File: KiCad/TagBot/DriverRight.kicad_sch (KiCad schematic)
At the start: 3 parts, among them U301 ZXBM5210-SP

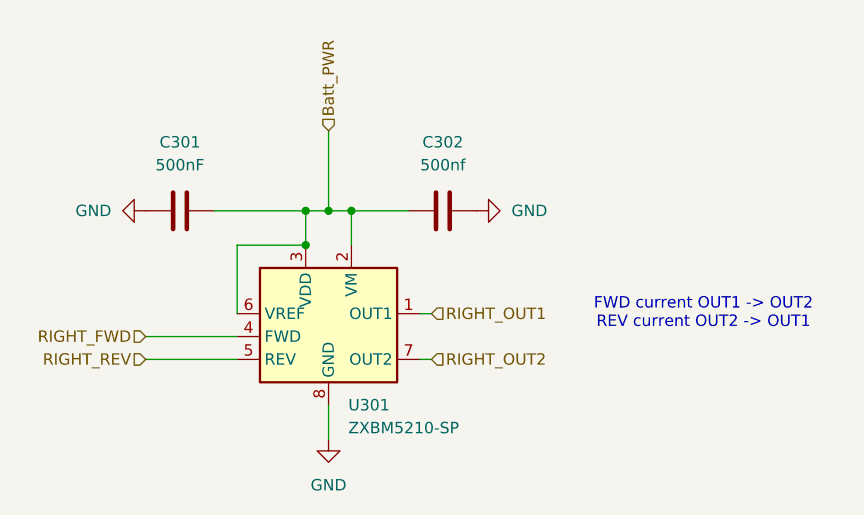
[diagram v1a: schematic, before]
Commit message: update footprint kicad
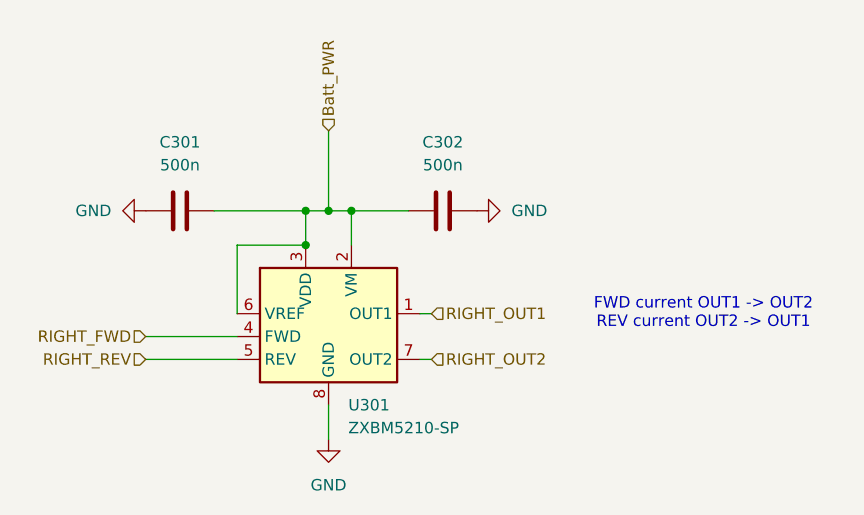
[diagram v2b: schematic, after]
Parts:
- C301: value 500nF -> 500n; footprint (none) -> Capacitor_SMD:C_0402_1005Metric
- C302: value 500nf -> 500n; footprint (none) -> Capacitor_SMD:C_0402_1005Metric
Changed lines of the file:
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@@
 			)
 		)
-		(property "Value" "500nf"
+		(property "Value" "500n"
 			(at 153.67 68.58 90)
 			(effects
@@
 			)
 		)
-		(property "Footprint" ""
+		(property "Footprint" "Capacitor_SMD:C_0402_1005Metric"
 			(at 149.86 74.6252 0)
 			(effects
@@
 			)
 		)
-		(property "Value" "500nF"
+		(property "Value" "500n"
 			(at 124.46 68.58 90)
 			(effects
@@
 			)
 		)
-		(property "Footprint" ""
+		(property "Footprint" "Capacitor_SMD:C_0402_1005Metric"
 			(at 128.27 72.6948 0)
 			(effects

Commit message: correction schema kicad
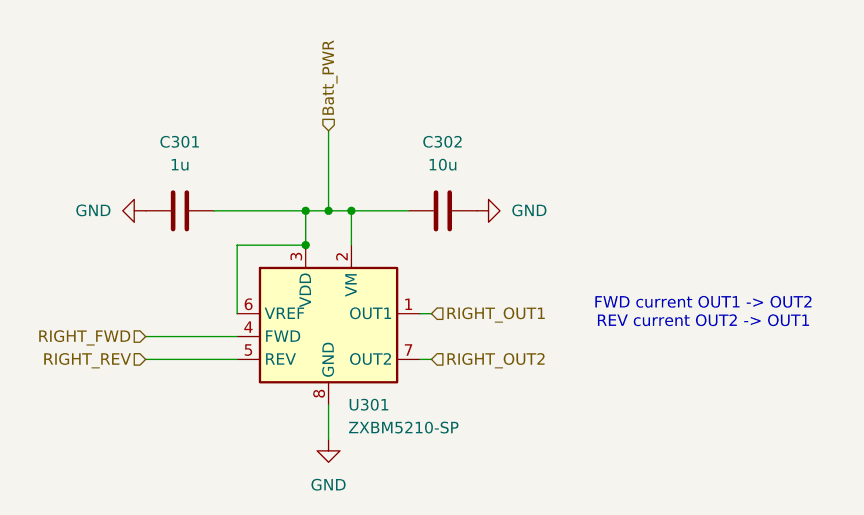
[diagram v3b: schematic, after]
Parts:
- C301: value 500n -> 1u
- C302: value 500n -> 10u
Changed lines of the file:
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@@
 			)
 		)
-		(property "Value" "500n"
+		(property "Value" "10u"
 			(at 153.67 68.58 90)
 			(effects
@@
 			)
 		)
-		(property "Value" "500n"
+		(property "Value" "1u"
 			(at 124.46 68.58 90)
 			(effects

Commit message: update routage
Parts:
- added TP3, TP4: TestPoint, TestPoint:TestPoint_Pad_D1.5mm, symbol Connector:TestPoint
- C301, C302: footprint Capacitor_SMD:C_0402_1005Metric -> Capacitor_SMD:C_0603_1608Metric
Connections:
- net RIGHT_FWD: now also TP3.1
- net RIGHT_REV: now also TP4.1
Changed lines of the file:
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@@
+	)
+	(junction
+		(at 123.19 90.17)
+		(diameter 0)
+		(color 0 0 0 0)
 	)
 	(junction
@@
 		(color 0 0 0 0)
 	)
+	(junction
+		(at 123.19 87.63)
+		(diameter 0)
+		(color 0 0 0 0)
+	)
 	(wire
 		(pts
@@
 	(wire
 		(pts
-			(xy 120.65 90.17) (xy 130.81 90.17)
+			(xy 120.65 90.17) (xy 123.19 90.17)
 		)
 		(stroke
@@
 	(wire
 		(pts
+			(xy 123.19 90.17) (xy 130.81 90.17)
+		)
+		(stroke
+			(width 0)
+			(type default)
+		)
+	)
+	(wire
+		(pts
 			(xy 140.97 95.25) (xy 140.97 99.06)
 		)
@@
 	(wire
 		(pts
-			(xy 120.65 87.63) (xy 130.81 87.63)
+			(xy 120.65 87.63) (xy 123.19 87.63)
 		)
 		(stroke
@@
 		(pts
 			(xy 140.97 73.66) (xy 140.97 64.77)
+		)
+		(stroke
+			(width 0)
+			(type default)
+		)
+	)
+	(wire
+		(pts
+			(xy 123.19 87.63) (xy 130.81 87.63)
 		)
 		(stroke
@@
 			)
 		)
-		(property "Footprint" "Capacitor_SMD:C_0402_1005Metric"
+		(property "Footprint" "Capacitor_SMD:C_0603_1608Metric"
 			(at 149.86 74.6252 0)
 			(effects
@@
 	)
 	(symbol
+		(lib_id "Connector:TestPoint")
+		(at 123.19 87.63 0)
+		(unit 1)
+		(exclude_from_sim no)
+		(in_bom yes)
+		(on_board yes)
+		(dnp no)
+		(fields_autoplaced yes)
+		(property "Reference" "TP3"
+			(at 125.73 83.0579 0)
+			(effects
+				(font
+					(size 1.27 1.27)
+				)
+				(justify left)
+			)
+		)
+		(property "Value" "TestPoint"
+			(at 125.73 85.5979 0)
+			(effects
+				(font
+					(size 1.27 1.27)
+				)
+				(justify left)
+			)
+		)
+		(property "Footprint" "TestPoint:TestPoint_Pad_D1.5mm"
+			(at 128.27 87.63 0)
+			(effects
+				(font
+					(size 1.27 1.27)
+				)
+				(hide yes)
+			)
+		)
+		(property "Datasheet" "~"
+			(at 128.27 87.63 0)
+			(effects
+				(font
+					(size 1.27 1.27)
+				)
+				(hide yes)
+			)
+		)
+		(property "Description" "test point"
+			(at 123.19 87.63 0)
+			(effects
+				(font
+					(size 1.27 1.27)
+				)
+				(hide yes)
+			)
+		)
+		(pin "1"
+		)
+		(instances
+			(project "TagBot"
+				(path "/6db08f37-7cb3-4000-93f1-ba0d0ffbeb19/4de9ab2c-d9ad-4c73-a2d5-dcacc317a2ed"
+					(reference "TP3")
+					(unit 1)
+				)
+			)
+		)
+	)
+	(symbol
+		(lib_id "Connector:TestPoint")
+		(at 123.19 90.17 180)
+		(unit 1)
+		(exclude_from_sim no)
+		(in_bom yes)
+		(on_board yes)
+		(dnp no)
+		(fields_autoplaced yes)
+		(property "Reference" "TP4"
+			(at 125.73 92.2019 0)
+			(effects
+				(font
+					(size 1.27 1.27)
+				)
+				(justify right)
+			)
+		)
+		(property "Value" "TestPoint"
+			(at 125.73 94.7419 0)
+			(effects
+				(font
+					(size 1.27 1.27)
+				)
+				(justify right)
+			)
+		)
+		(property "Footprint" "TestPoint:TestPoint_Pad_D1.5mm"
+			(at 118.11 90.17 0)
+			(effects
+				(font
+					(size 1.27 1.27)
+				)
+				(hide yes)
+			)
+		)
+		(property "Datasheet" "~"
+			(at 118.11 90.17 0)
+			(effects
+				(font
+					(size 1.27 1.27)
+				)
+				(hide yes)
+			)
+		)
+		(property "Description" "test point"
+			(at 123.19 90.17 0)
+			(effects
+				(font
+					(size 1.27 1.27)
+				)
+				(hide yes)
+			)
+		)
+		(pin "1"
+		)
+		(instances
+			(project "TagBot"
+				(path "/6db08f37-7cb3-4000-93f1-ba0d0ffbeb19/4de9ab2c-d9ad-4c73-a2d5-dcacc317a2ed"
+					(reference "TP4")
+					(unit 1)
+				)
+			)
+		)
+	)
+	(symbol
 		(lib_id "Device:C")
 		(at 124.46 73.66 90)
@@
 			)
 		)
-		(property "Footprint" "Capacitor_SMD:C_0402_1005Metric"
+		(property "Footprint" "Capacitor_SMD:C_0603_1608Metric"
 			(at 128.27 72.6948 0)
 			(effects

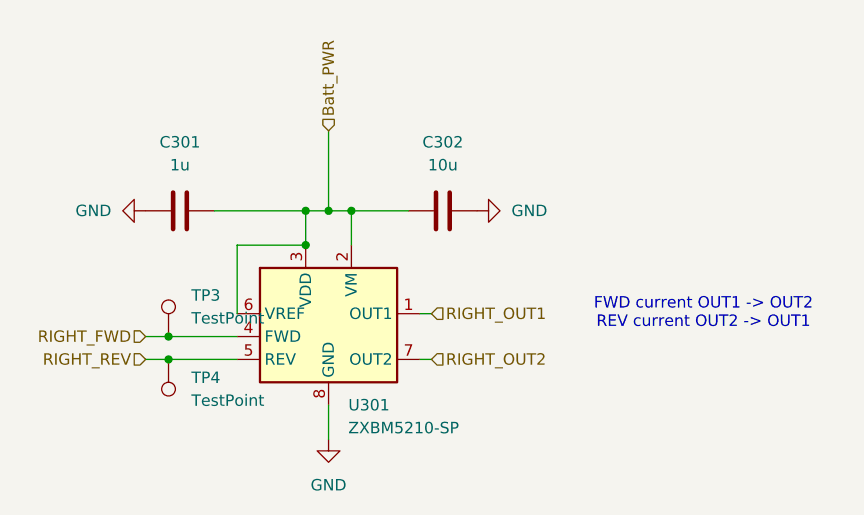
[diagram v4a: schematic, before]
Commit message: fixed switch footprint and genrated gerber files
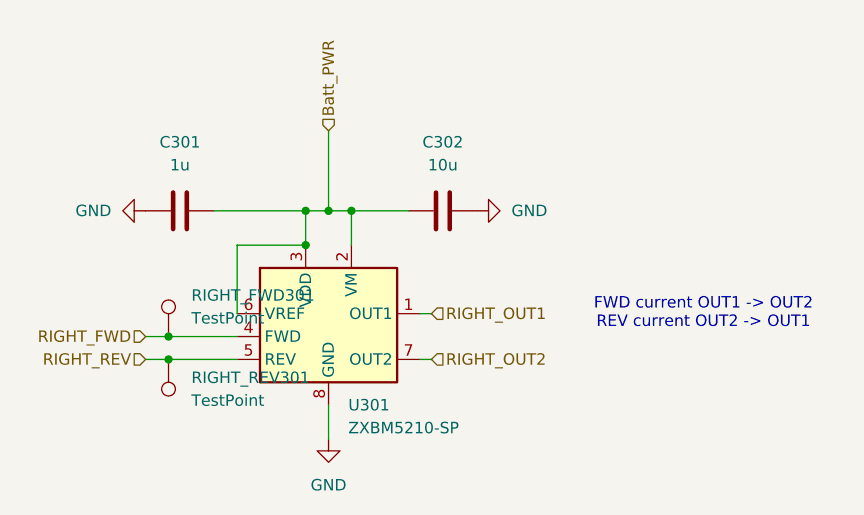
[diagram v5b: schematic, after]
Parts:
- renumbered TP3 to RIGHT_FWD301, TP4 to RIGHT_REV301
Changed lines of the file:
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@@
 		(dnp no)
 		(fields_autoplaced yes)
-		(property "Reference" "TP3"
+		(property "Reference" "RIGHT_FWD301"
 			(at 125.73 83.0579 0)
 			(effects
@@
 			(project "TagBot"
 				(path "/6db08f37-7cb3-4000-93f1-ba0d0ffbeb19/4de9ab2c-d9ad-4c73-a2d5-dcacc317a2ed"
-					(reference "TP3")
+					(reference "RIGHT_FWD301")
 					(unit 1)
 				)
@@
 		(dnp no)
 		(fields_autoplaced yes)
-		(property "Reference" "TP4"
+		(property "Reference" "RIGHT_REV301"
 			(at 125.73 92.2019 0)
 			(effects
@@
 			(project "TagBot"
 				(path "/6db08f37-7cb3-4000-93f1-ba0d0ffbeb19/4de9ab2c-d9ad-4c73-a2d5-dcacc317a2ed"
-					(reference "TP4")
+					(reference "RIGHT_REV301")
 					(unit 1)
 				)
